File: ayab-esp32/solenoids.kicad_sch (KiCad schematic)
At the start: 6 parts

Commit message: fix folder structure and update gitignore
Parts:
- C301, C302, C303: symbol Device:C_Small -> ayab-esp32:C_Small
- U? (x3): symbol Transistor_Array:ULN2003A -> ayab-esp32:ULN2003A
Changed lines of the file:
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@@
     )
   )
-  (symbol (lib_id "Device:C_Small") (at 228.6 55.88 0) (unit 1)
+  (symbol (lib_id "ayab-esp32:C_Small") (at 228.6 55.88 0) (unit 1)
     (in_bom yes) (on_board yes) (dnp no)
     (property "Reference" "C303" (at 231.14 54.6163 0)
@@
     )
   )
-  (symbol (lib_id "Device:C_Small") (at 132.08 55.88 0) (unit 1)
+  (symbol (lib_id "ayab-esp32:C_Small") (at 132.08 55.88 0) (unit 1)
     (in_bom yes) (on_board yes) (dnp no)
     (property "Reference" "C301" (at 134.62 54.6163 0)
@@
     )
   )
-  (symbol (lib_id "Transistor_Array:ULN2003A") (at 101.6 62.23 0) (unit 1)
+  (symbol (lib_id "ayab-esp32:ULN2003A") (at 101.6 62.23 0) (unit 1)
     (in_bom yes) (on_board yes) (dnp no) (fields_autoplaced)
     (property "Reference" "U?" (at 101.6 45.72 0)
@@
     )
   )
-  (symbol (lib_id "Device:C_Small") (at 132.08 104.14 0) (unit 1)
+  (symbol (lib_id "ayab-esp32:C_Small") (at 132.08 104.14 0) (unit 1)
     (in_bom yes) (on_board yes) (dnp no)
     (property "Reference" "C302" (at 134.62 102.8763 0)
@@
     )
   )
-  (symbol (lib_id "Transistor_Array:ULN2003A") (at 101.6 110.49 0) (unit 1)
+  (symbol (lib_id "ayab-esp32:ULN2003A") (at 101.6 110.49 0) (unit 1)
     (in_bom yes) (on_board yes) (dnp no) (fields_autoplaced)
     (property "Reference" "U?" (at 101.6 93.98 0)
@@
     )
   )
-  (symbol (lib_id "Transistor_Array:ULN2003A") (at 198.12 62.23 0) (unit 1)
+  (symbol (lib_id "ayab-esp32:ULN2003A") (at 198.12 62.23 0) (unit 1)
     (in_bom yes) (on_board yes) (dnp no) (fields_autoplaced)
     (property "Reference" "U?" (at 198.12 45.72 0)

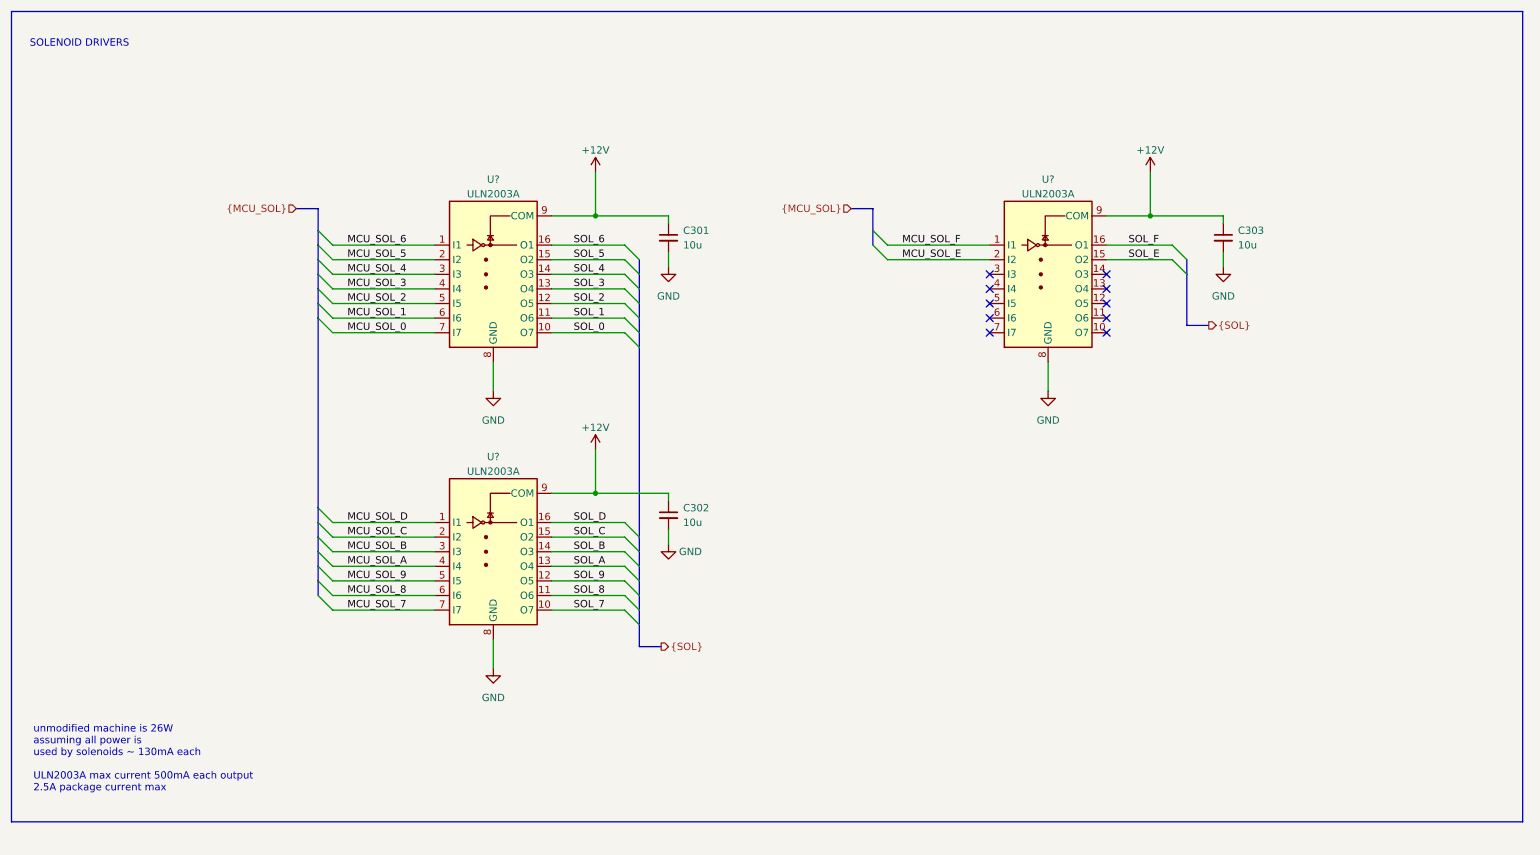
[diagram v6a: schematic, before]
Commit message: refactor for i2c expander
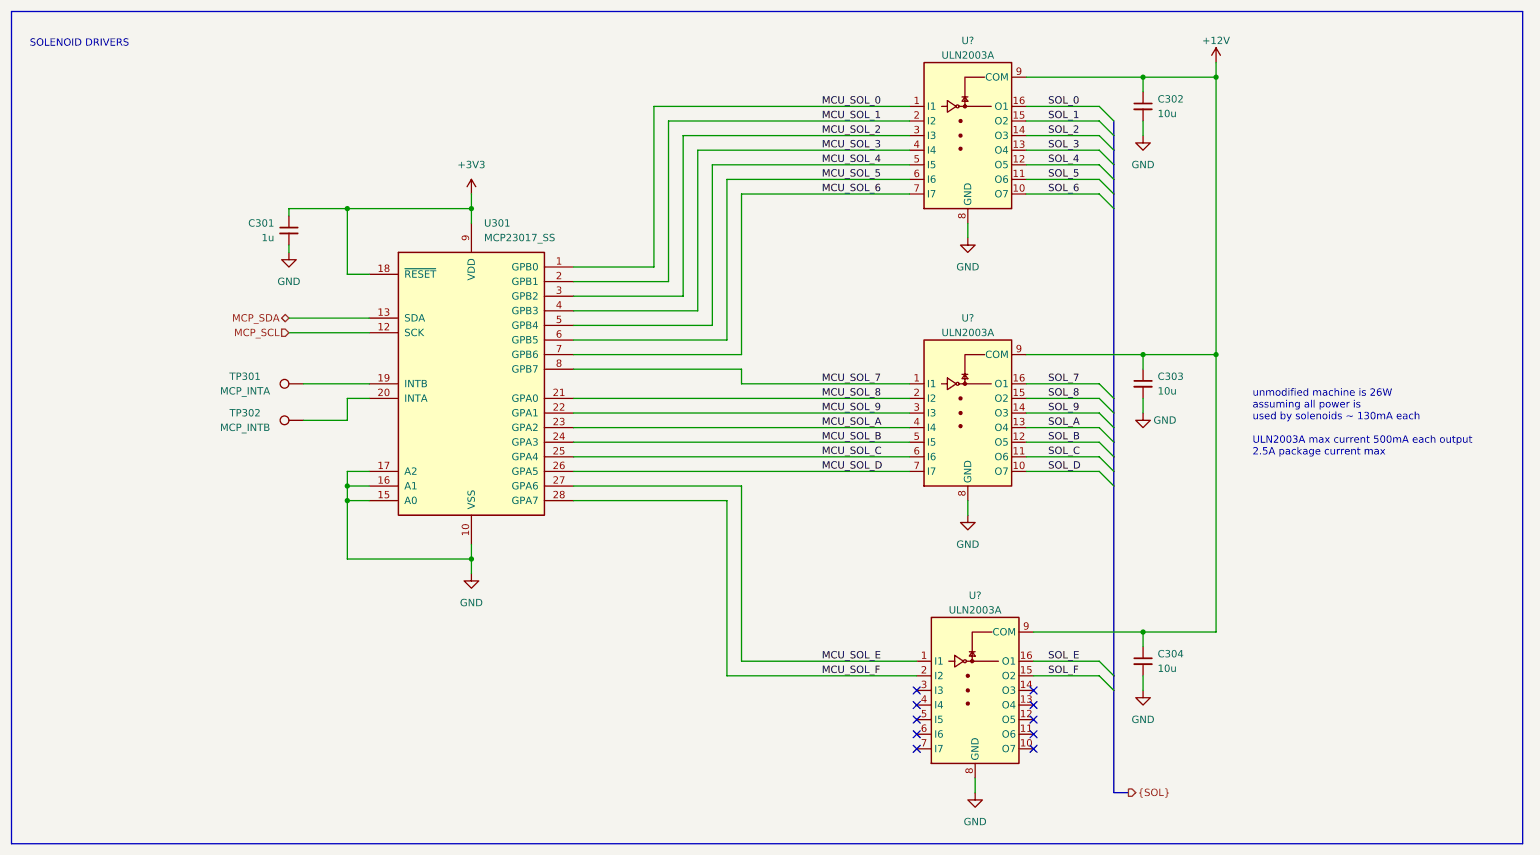
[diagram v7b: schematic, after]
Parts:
- added C301: 1u, symbol ayab-esp32:C_Small
- added TP301: MCP_INTA, symbol ayab-esp32:TestPoint
- added TP302: MCP_INTB, symbol ayab-esp32:TestPoint
- added U301: MCP23017_SS, Package_SO:SSOP-28_5.3x10.2mm_P0.65mm, symbol Interface_Expansion:MCP23017_SS
- renumbered C301 to C302, C302 to C303, C303 to C304
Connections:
- net GND: now also C301.2, U301.10 (VSS), U301.15 (A0), U301.16 (A1), U301.17 (A2)
- net MCU_SOL_0: now also U?.1 (I1), U301.1 (GPB0); no longer U?.7 (I7)
- net MCU_SOL_1: now also U?.2 (I2), U301.2 (GPB1); no longer U?.6 (I6)
- net MCU_SOL_2: now also U?.3 (I3), U301.3 (GPB2); no longer U?.5 (I5)
- net MCU_SOL_3: now also U301.4 (GPB3)
- net MCU_SOL_4: now also U?.5 (I5), U301.5 (GPB4); no longer U?.3 (I3)
- net MCU_SOL_5: now also U?.6 (I6), U301.6 (GPB5); no longer U?.2 (I2)
- net MCU_SOL_6: now also U?.7 (I7), U301.7 (GPB6); no longer U?.1 (I1)
- net MCU_SOL_7: now also U?.1 (I1), U301.8 (GPB7); no longer U?.7 (I7)
- net MCU_SOL_8: now also U?.2 (I2), U301.21 (GPA0); no longer U?.6 (I6)
- net MCU_SOL_9: now also U?.3 (I3), U301.22 (GPA1); no longer U?.5 (I5)
- net MCU_SOL_A: now also U301.23 (GPA2)
- net MCU_SOL_B: now also U?.5 (I5), U301.24 (GPA3); no longer U?.3 (I3)
- net MCU_SOL_C: now also U?.6 (I6), U301.25 (GPA4); no longer U?.2 (I2)
- net MCU_SOL_D: now also U?.7 (I7), U301.26 (GPA5); no longer U?.1 (I1)
- net MCU_SOL_E: now also U?.1 (I1), U301.27 (GPA6); no longer U?.2 (I2)
- net MCU_SOL_F: now also U?.2 (I2), U301.28 (GPA7); no longer U?.1 (I1)
- net SOL_0: now also U?.16 (O1); no longer U?.10 (O7)
- net SOL_1: now also U?.15 (O2); no longer U?.11 (O6)
- net SOL_2: now also U?.14 (O3); no longer U?.12 (O5)
- net SOL_4: now also U?.12 (O5); no longer U?.14 (O3)
- net SOL_5: now also U?.11 (O6); no longer U?.15 (O2)
- net SOL_6: now also U?.10 (O7); no longer U?.16 (O1)
- net SOL_7: now also U?.16 (O1); no longer U?.10 (O7)
- net SOL_8: now also U?.15 (O2); no longer U?.11 (O6)
- net SOL_9: now also U?.14 (O3); no longer U?.12 (O5)
- net SOL_B: now also U?.12 (O5); no longer U?.14 (O3)
- net SOL_C: now also U?.11 (O6); no longer U?.15 (O2)
- net SOL_D: now also U?.10 (O7); no longer U?.16 (O1)
- net SOL_E: now also U?.16 (O1); no longer U?.15 (O2)
- net SOL_F: now also U?.15 (O2); no longer U?.16 (O1)
- new net: TP301.1, U301.19 (INTB)
- new net: TP302.1, U301.20 (INTA)
- new net +3V3: C301.1, U301.18 (~{RESET}), U301.9 (VDD)
- new net MCP_SCL: U301.12 (SCK)
- new net MCP_SDA: U301.13 (SDA)
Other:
- moved on the sheet: C302, C303, C304, U?

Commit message: update local library + pdf
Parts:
- U301: symbol Interface_Expansion:MCP23017_SS -> ayab-esp32:MCP23017_SS
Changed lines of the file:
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@@
     )
   )
-  (symbol (lib_id "Interface_Expansion:MCP23017_SS") (at 97.79 81.28 0) (unit 1)
+  (symbol (lib_id "ayab-esp32:MCP23017_SS") (at 97.79 81.28 0) (unit 1)
     (in_bom yes) (on_board yes) (dnp no) (fields_autoplaced)
     (property "Reference" "U301" (at 99.9841 53.34 0)
